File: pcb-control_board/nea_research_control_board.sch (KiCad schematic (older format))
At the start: 7 parts

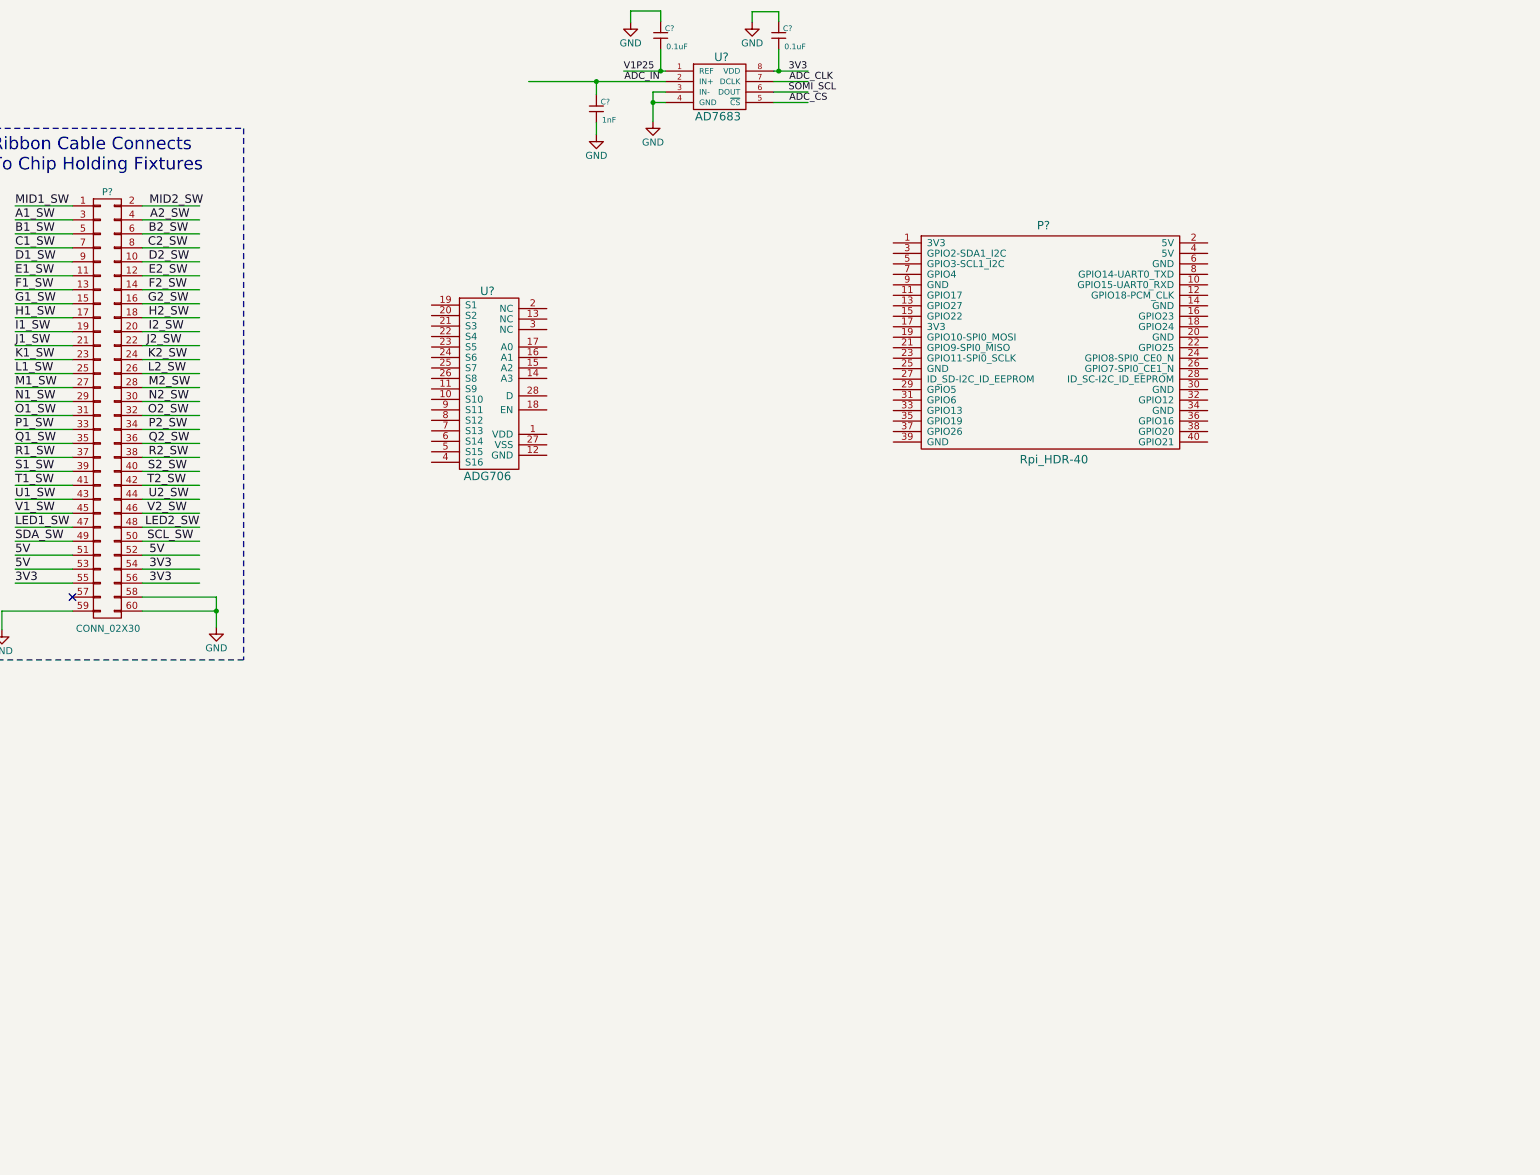
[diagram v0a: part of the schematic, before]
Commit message: -removed solder paste layer from breakout board bond pad footprint -starting on control board schematic
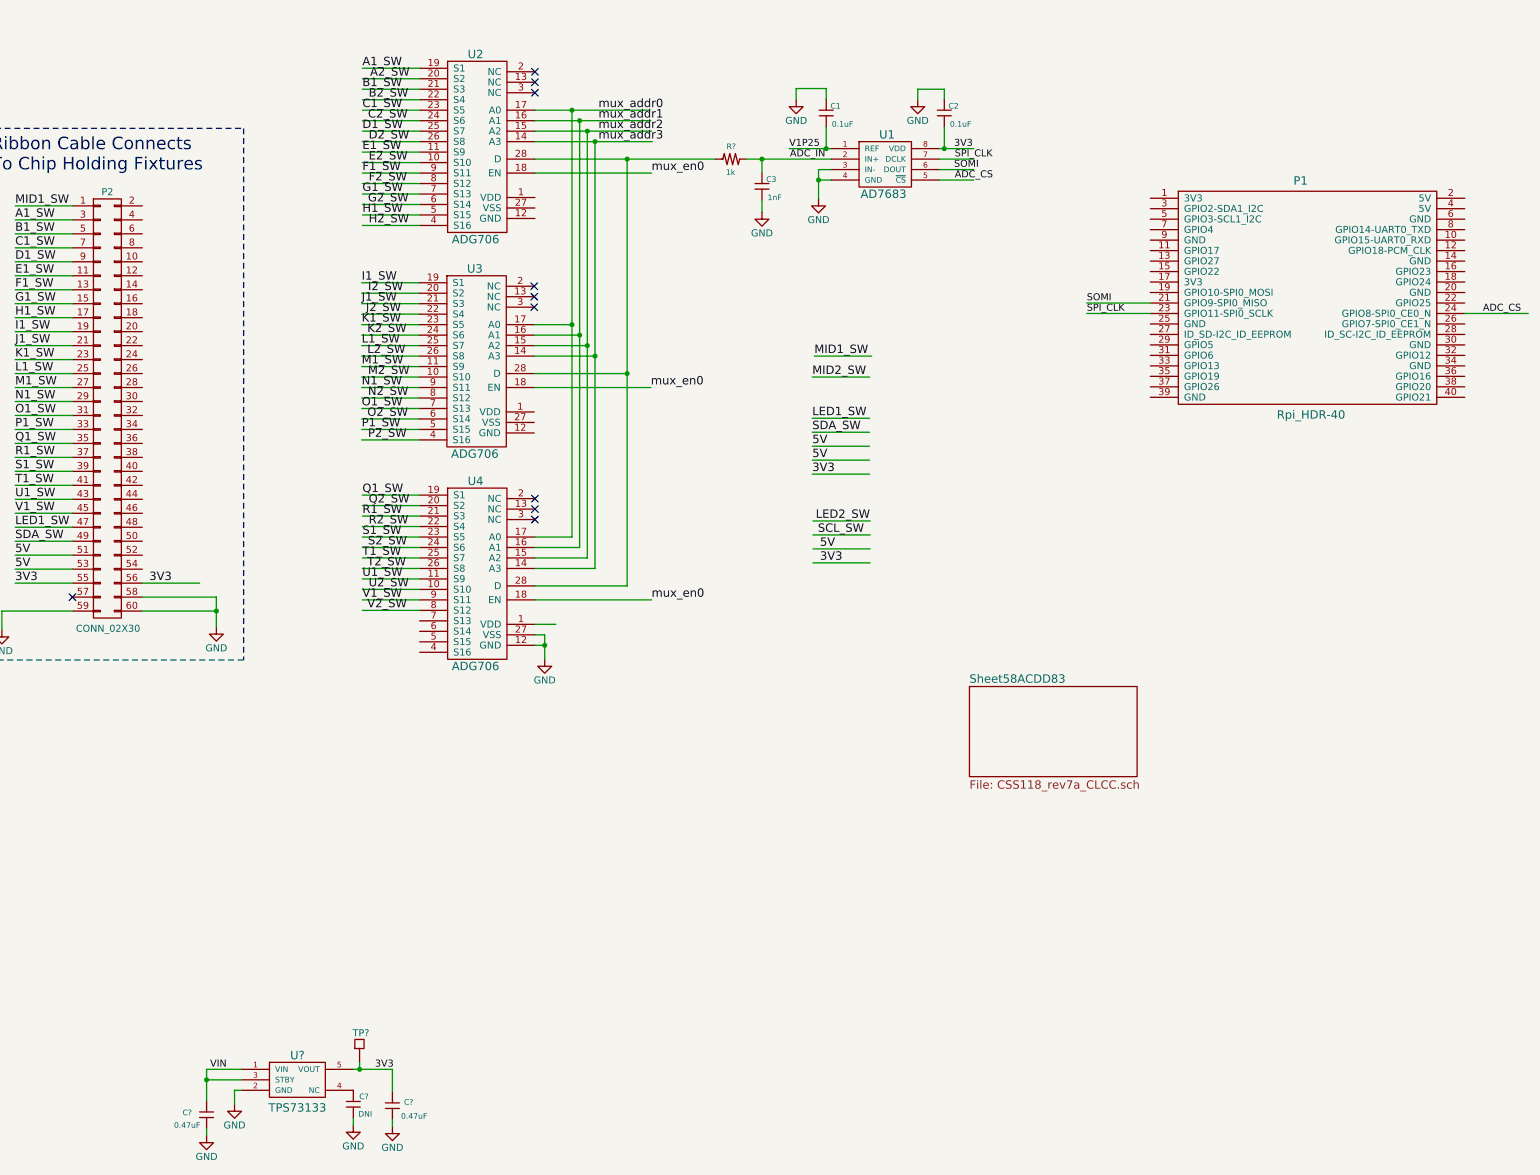
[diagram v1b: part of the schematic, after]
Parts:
- added C? (x2): 0.47uF, footprints_on_Cdrive:0402, symbol CAP_NP
- added C?: DNI, footprints_on_Cdrive:0402, symbol CAP_NP
- added R?: 1k, footprints_on_Cdrive:0603_sm, symbol Res1_1
- added TP?: probe_point, footprints_on_Cdrive:probe_point, symbol probe_point
- added U3, U4: ADG706, symbol ADG706
- added U?: TPS73133, footprints_on_Cdrive:SOT23-5, symbol BU33TD3WG
- gave numbers to parts that had none: 7
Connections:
- net labels added: SOMI, SPI_CLK, VIN, mux_addr0, mux_addr1, mux_addr2, mux_addr3, mux_en0
- net labels removed: ADC_CLK, SOMI_SCL
- wire segments 80 -> 149
- no-connect marks 1 -> 10
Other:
- moved on the sheet: C1, C2, C3, P1, U1, U2

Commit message: -added adc mux and gnd mux to control board schematic
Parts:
- added U5, U6, U7: ADG706, symbol ADG706
- gave numbers to parts that had none: 6
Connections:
- net labels added: 3V3_Rpi, 5V_Rpi, CLK, SCL, SDA, SIMO, gnd_addr0, gnd_addr1, gnd_addr2, gnd_addr3, gnd_en0, ~CS_SW
- net labels removed: SDA_SW, SPI_CLK, VIN
- wire segments 149 -> 264
- no-connect marks 10 -> 26
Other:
- note added: "Select Signal For ADC Measurement"
- note added: "Select Signal To Gnd If Required"
- moved on the sheet: C4, C5, C6, P1, TP1, U8
